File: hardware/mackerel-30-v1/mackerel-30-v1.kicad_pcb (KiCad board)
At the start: 4 copper layers, 210 x 150 mm, 141 parts, among them J1 Conn_02x05_Odd_Even, J10 Conn_01x06, J11 Conn_02x20_Odd_Even, J12 Conn_02x40_Odd_Even, J2 Conn_02x05_Odd_Even, J3 Barrel_Jack_MountingPin, J4 Conn_02x03_Odd_Even, J5 Conn_02x03_Odd_Even, J6 DE9_Socket_MountingHoles, J7 DE9_Pins_MountingHoles, J8 Conn_02x10_Odd_Even, J9 Conn_01x06, SW1 SW_Push, U1 MC68030RC, U10 DS1233, U11 MAX232, U12 MAX232, U13 XR68C681, U14 SST39SF040, U15 74ABT245, U16 AS6C4008-55PCN, U17 MC68882, U18 74HC245, U19 74HC245, U2 EPM7128, U20 SN74LVC8T245, U21 SN74LVC8T245, U22 SN74LVC8T245, U23 SN74LVC8T245, U24 SN74LVC8T245, U25 SN74LVC8T245, U26 SN74LVC8T245, U3 EPM7128, U4 SIMM72, U5 74ABT245, U6 74ABT245, U7 74ABT245, U8 74ABT245, U9 LM2576T-5, X1 24 MHz, X2 50 MHz, X3 3.6864MHz

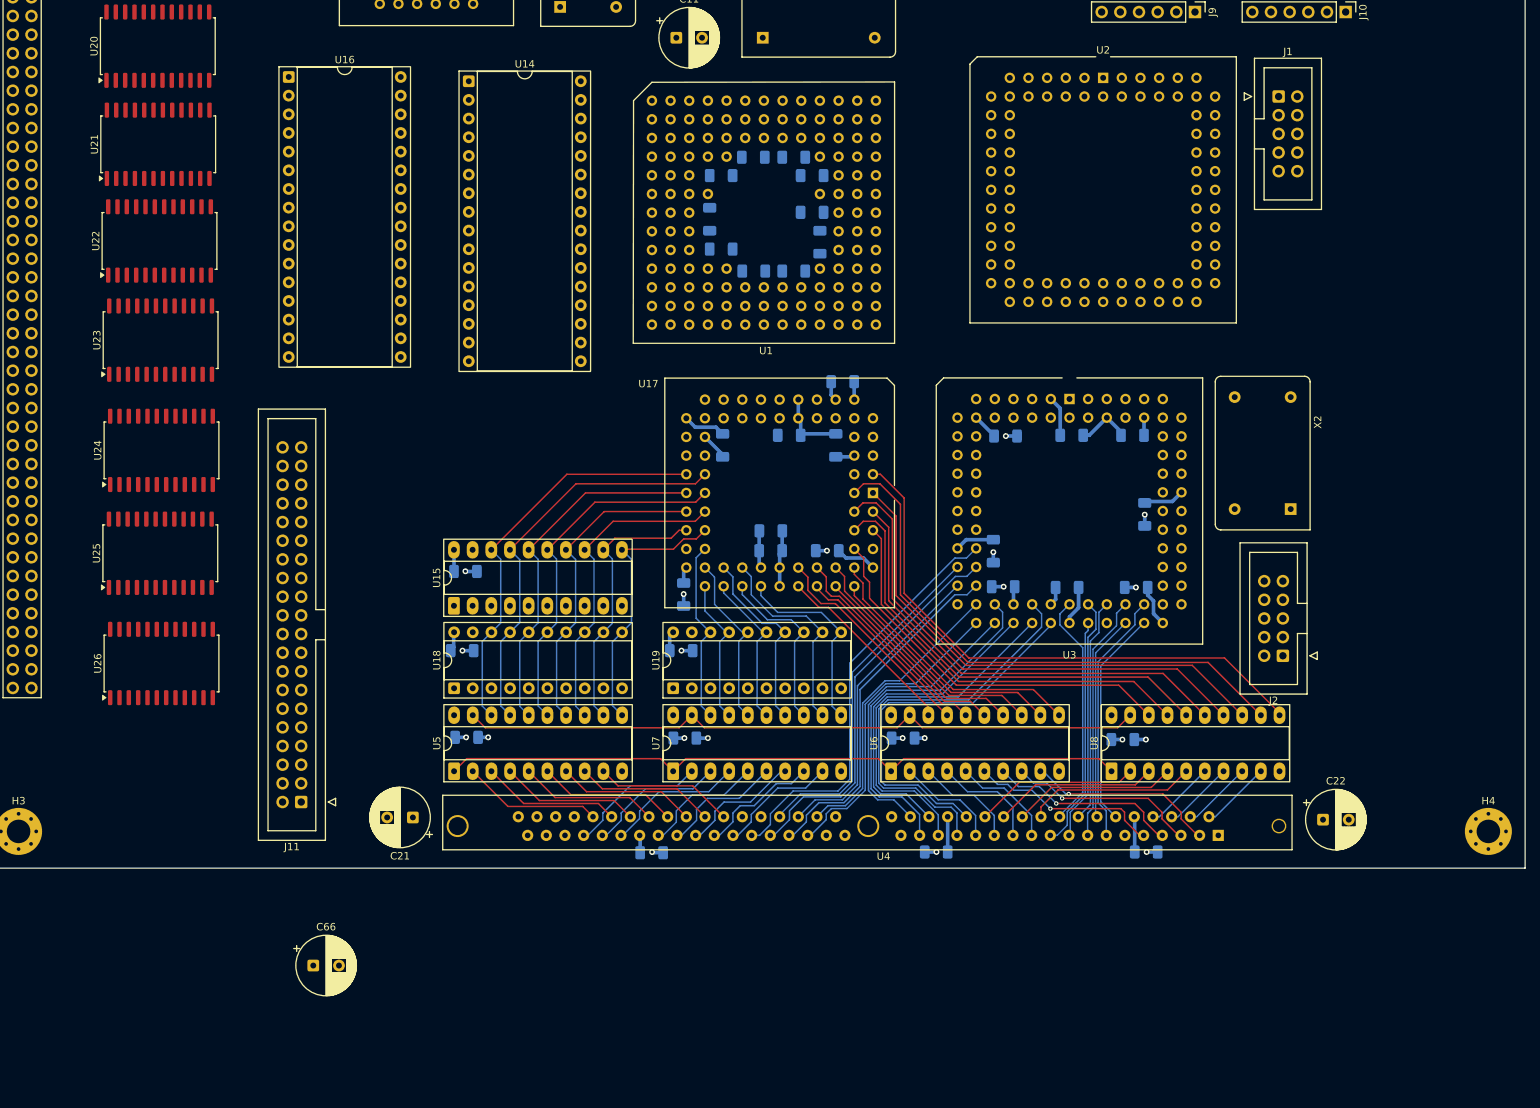
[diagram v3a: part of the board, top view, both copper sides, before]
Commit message: Mackerel-30: More data bus routing
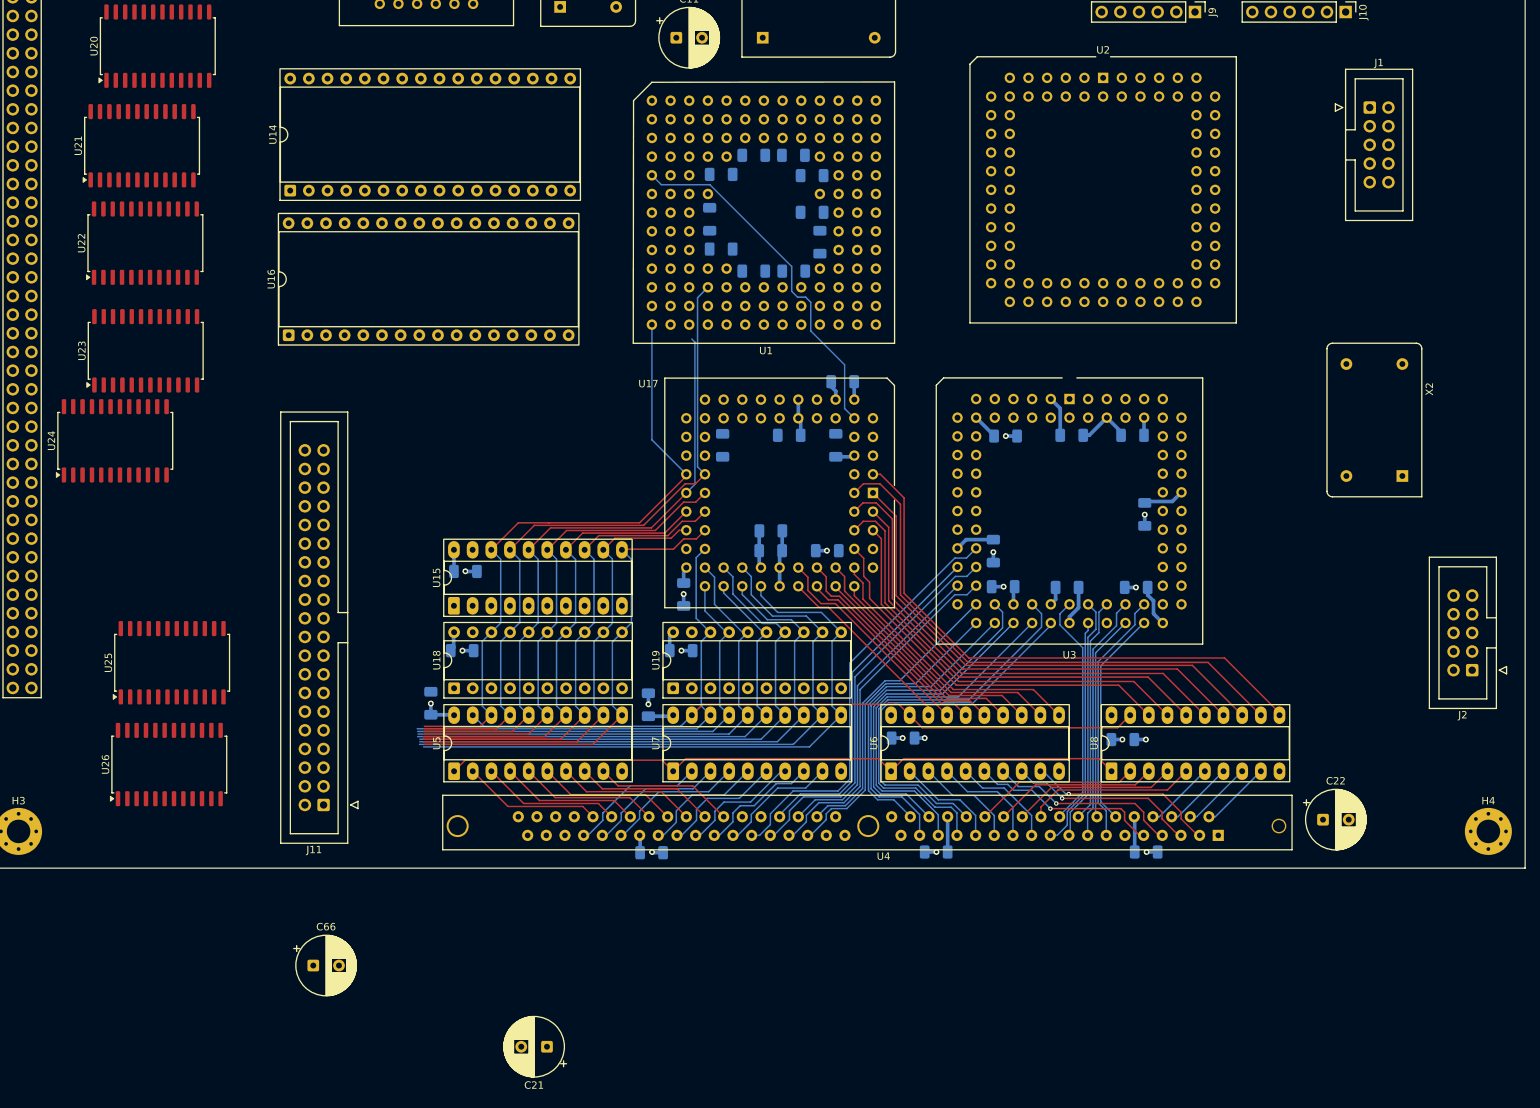
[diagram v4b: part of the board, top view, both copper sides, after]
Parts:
- moved C21 36.1 mm to (96.9, 194.3)
- moved U16 35.1 mm to (61.8, 97.5), turned to 90 degrees
- moved U14 28.5 mm to (62.0, 77.8), turned to 90 degrees
- moved J2 25.8 mm to (222.8, 143.1)
- moved X2 15.9 mm to (213.3, 116.6)
- moved U25 15.0 mm to (45.9, 142.1)
- moved U26 13.8 mm to (45.5, 155.9)
- moved J1 12.5 mm to (208.9, 66.5)
- moved C35 6.72 mm to (110.7, 147.8), turned to 90 degrees
- moved C34 6.72 mm to (81.1, 147.6), turned to 90 degrees
- moved U24 6.42 mm to (38.2, 111.8)
- moved J11 3.07 mm to (66.5, 161.4)
- moved U23 2.49 mm to (42.3, 99.6)
- moved U21 2.21 mm to (41.8, 71.7)
- moved U22 1.94 mm to (42.3, 85.0)
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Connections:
- U20 pad 1: unconnected-(U20-V_{CCA}-Pad1) -> +5V
- U20 pad 11: Net-(U20-GND-Pad11) -> GND
- U20 pad 12: Net-(U20-GND-Pad11) -> GND
- U20 pad 13: Net-(U20-GND-Pad11) -> GND
- U21 pad 1: unconnected-(U21-V_{CCA}-Pad1) -> +5V
- U21 pad 11: Net-(U21-GND-Pad11) -> GND
- U21 pad 12: Net-(U21-GND-Pad11) -> GND
- U21 pad 13: Net-(U21-GND-Pad11) -> GND
- U22 pad 1: unconnected-(U22-V_{CCA}-Pad1) -> +5V
- U22 pad 10: unconnected-(U22-A8-Pad10) -> A23
- U22 pad 11: Net-(U22-GND-Pad11) -> GND
- U22 pad 12: Net-(U22-GND-Pad11) -> GND
- U22 pad 13: Net-(U22-GND-Pad11) -> GND
- U22 pad 3: unconnected-(U22-A1-Pad3) -> A16
- U22 pad 4: unconnected-(U22-A2-Pad4) -> A17
- U22 pad 5: unconnected-(U22-A3-Pad5) -> A18
- U22 pad 6: unconnected-(U22-A4-Pad6) -> A19
- U22 pad 7: unconnected-(U22-A5-Pad7) -> A20
- U22 pad 8: unconnected-(U22-A6-Pad8) -> A21
- U22 pad 9: unconnected-(U22-A7-Pad9) -> A22
- U23 pad 1: unconnected-(U23-V_{CCA}-Pad1) -> +5V
- U23 pad 10: unconnected-(U23-A8-Pad10) -> A15
- U23 pad 11: Net-(U23-GND-Pad11) -> GND
- U23 pad 12: Net-(U23-GND-Pad11) -> GND
- U23 pad 13: Net-(U23-GND-Pad11) -> GND
- U23 pad 3: unconnected-(U23-A1-Pad3) -> A8
- U23 pad 4: unconnected-(U23-A2-Pad4) -> A9
- U23 pad 5: unconnected-(U23-A3-Pad5) -> A10
- U23 pad 6: unconnected-(U23-A4-Pad6) -> A11
- U23 pad 7: unconnected-(U23-A5-Pad7) -> A12
- U23 pad 8: unconnected-(U23-A6-Pad8) -> A13
- U23 pad 9: unconnected-(U23-A7-Pad9) -> A14
- U24 pad 1: unconnected-(U24-V_{CCA}-Pad1) -> +5V
- U24 pad 10: unconnected-(U24-A8-Pad10) -> A7
- U24 pad 11: Net-(U24-GND-Pad11) -> GND
- U24 pad 12: Net-(U24-GND-Pad11) -> GND
- U24 pad 13: Net-(U24-GND-Pad11) -> GND
- U24 pad 3: unconnected-(U24-A1-Pad3) -> A0
- U24 pad 4: unconnected-(U24-A2-Pad4) -> A1
- U24 pad 5: unconnected-(U24-A3-Pad5) -> A2
- U24 pad 6: unconnected-(U24-A4-Pad6) -> A3
- U24 pad 7: unconnected-(U24-A5-Pad7) -> A4
- U24 pad 8: unconnected-(U24-A6-Pad8) -> A5
- U24 pad 9: unconnected-(U24-A7-Pad9) -> A6
- U25 pad 1: unconnected-(U25-V_{CCA}-Pad1) -> +5V
- U25 pad 10: unconnected-(U25-A8-Pad10) -> D23
- U25 pad 11: Net-(U25-GND-Pad11) -> GND
- U25 pad 12: Net-(U25-GND-Pad11) -> GND
- U25 pad 13: Net-(U25-GND-Pad11) -> GND
- U25 pad 3: unconnected-(U25-A1-Pad3) -> D16
- U25 pad 4: unconnected-(U25-A2-Pad4) -> D17
- U25 pad 5: unconnected-(U25-A3-Pad5) -> D18
- U25 pad 6: unconnected-(U25-A4-Pad6) -> D19
- U25 pad 7: unconnected-(U25-A5-Pad7) -> D20
- U25 pad 8: unconnected-(U25-A6-Pad8) -> D21
- U25 pad 9: unconnected-(U25-A7-Pad9) -> D22
- U26 pad 1: unconnected-(U26-V_{CCA}-Pad1) -> +5V
- U26 pad 10: unconnected-(U26-A8-Pad10) -> D31
- U26 pad 11: Net-(U26-GND-Pad11) -> GND
- U26 pad 12: Net-(U26-GND-Pad11) -> GND
- U26 pad 13: Net-(U26-GND-Pad11) -> GND
- U26 pad 3: unconnected-(U26-A1-Pad3) -> D24
- U26 pad 4: unconnected-(U26-A2-Pad4) -> D25
- U26 pad 5: unconnected-(U26-A3-Pad5) -> D26
- U26 pad 6: unconnected-(U26-A4-Pad6) -> D27
- U26 pad 7: unconnected-(U26-A5-Pad7) -> D28
- U26 pad 8: unconnected-(U26-A6-Pad8) -> D29
- U26 pad 9: unconnected-(U26-A7-Pad9) -> D30
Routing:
- net D16: track 26.6 -> 85.2 mm
- net D17: track 28.4 -> 84.8 mm
- net D18: track 24.0 -> 77.7 mm
- net D19: track 25.8 -> 76.8 mm
- net CLK_CPU: track 0.00 -> 49.0 mm
- net D20: track 21.3 -> 70.0 mm
- net D21: track 24.0 -> 69.9 mm
- net D22: track 20.2 -> 63.5 mm
- net D23: track 25.0 -> 65.7 mm
- net D30: track 55.5 -> 94.4 mm
- net D29: track 49.3 -> 86.0 mm
- net D31: track 55.4 -> 87.6 mm
- net D24: track 37.1 -> 65.6 mm
- net D25: track 37.0 -> 63.0 mm
- net D26: track 43.1 -> 66.4 mm
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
